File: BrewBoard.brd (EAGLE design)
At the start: 69.2 x 20.3 mm, 23 parts, among them J1 BATT, J2 AUX, J3 SPK, J5 PIXEL, J6 STAR, J7 MAIN, J8 String, Q1 2n7002k, Q2 2n7002k, Q3 2n7002k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

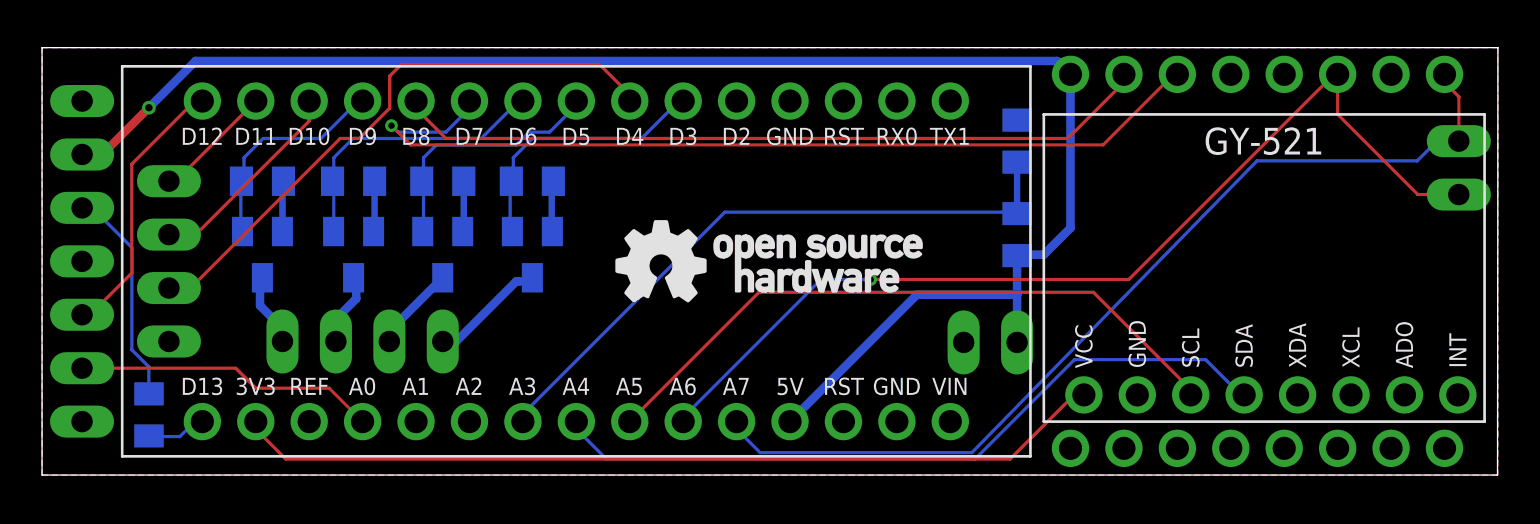
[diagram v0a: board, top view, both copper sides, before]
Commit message: Brewboard V3 Update
Adding New Version 3 Update of Brewboard
Feature/Change List;
- Interrupt mode is now available for clashes.
- All extra Pins have pads (for folks that want to experiment and add features).
- LED Power Traces are now able to handle a total of 7.8A so Pixel Blades can be safely hooked up to MOSFETs (less drain in deepsleep).
- Power Traces for Pixels removed! Pixel Blade can be wired directly from the battery Positive, and to two or three of the RGB MOSFET pads as mentioned above.
- 4th MOSFET removed to reduce part count.
- Pixel Data Line resistor removed, as it really should be on the blade side (also reduces part count).
- All Pins are now Labelled and should now be large enough to be readable.
- Added a few Vias for better overall grounds.
- Spiffy new logo!
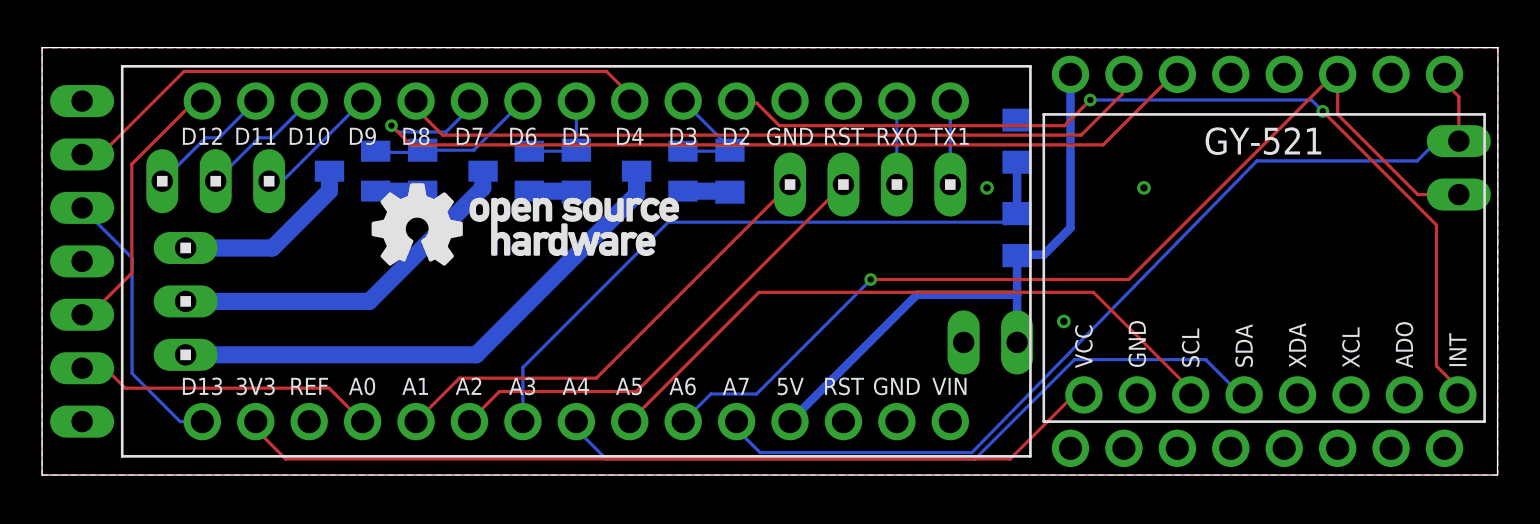
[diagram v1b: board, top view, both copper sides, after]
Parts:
- removed J2: AUX, BrewBoard:10X02MTA
- removed Q4: 2n7002k, BrewBoard:SOT23
- removed R4: 100k Ohms, BrewBoard:R0805
- removed R5: 220 Ohm, BrewBoard:R0805
- added J4: STAR, BrewBoard:10X03MTA
- added J9: COM, BrewBoard:10X02MTA
- J5: value PIXEL -> AUX
- J6: value STAR -> ANO; device BrewBoard:10X04MTA -> BrewBoard:10X02MTA
- J8: value String -> DIGI; device BrewBoard:10X02MTA -> BrewBoard:10X03MTA
- Q1, Q2, Q3: value 2n7002k -> si2302cds-t1-e3
- R6: value 100 kOhm -> 100k Ohms
- R7: value 470 kOhm -> 470k Ohms
- U$2: device BrewBoard:BREWBOARD-LOGO_VERYSMALL -> SaberRepublicLogos:BREWBOARD_GOLDSTAR_SM
- moved J6 22.8 mm to (36.8, 13.8), flipped to the top
- moved U$2 16.2 mm to (11.3, 4.45)
- moved U$3 11.7 mm to (15.7, 10.0)
- moved R1 9.40 mm to (32.7, 14.4), turned to 270 degrees
- moved Q3 7.24 mm to (29.4, 14.4), turned to 270 degrees
- moved R2 6.37 mm to (25.4, 14.4), turned to 270 degrees
- moved Q2 4.98 mm to (22.1, 14.4), turned to 270 degrees
- moved Q1 3.97 mm to (14.8, 14.4), turned to 270 degrees
- moved R3 3.32 mm to (18.1, 14.4), turned to 270 degrees
- moved J8 2.56 mm to (8.26, 14.0), flipped to the top, turned to 180 degrees
- renumbered U$1 to U3
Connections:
- net N$16 renamed D11
- net N$7 renamed D10
- removed net N$23: J6.2, Q1.3
- removed net N$24: J6.3, Q2.3
- removed net N$25: J6.4, Q3.3
- removed net N$28: J6.1, Q4.3
- removed net N$9: J5.3, R5.1
- new net A1: J6.2, U1.20
- new net A2: J6.1, U1.21
- new net D2: U1.5, U2.INT
- new net LS1: J4.3, Q3.3
- new net LS2: J4.2, Q2.3
- new net LS3: J4.1, Q1.3
- new net N$1: J9.2, U1.2
- new net N$2: J9.1, U1.1
- net +5V: no longer J5.2
- net 0: no longer J2.1, Q4.2, R4.2
- net D13: now also J5.3; no longer R5.2
- net D4: now also J5.2; no longer J2.2
- net D9: now also J8.3; no longer Q4.1, R4.1
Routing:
- net +5V: track 76.9 -> 27.8 mm, vias 1 -> 0
- net D2: track 0.00 -> 45.3 mm, vias 0 -> 2
- net LS1: track 0.00 -> 25.7 mm
- net A2: track 0.00 -> 22.4 mm
- net A1: track 0.00 -> 22.4 mm
- net LS2: track 0.00 -> 17.2 mm
- net N$9: track 10.6 -> 0.00 mm
- net D13: track 2.84 -> 13.1 mm
- net LS3: track 0.00 -> 8.90 mm
- net D3: track 12.9 -> 5.51 mm
- net D5: track 12.1 -> 5.25 mm
- net D6: track 13.7 -> 8.02 mm
- net N$25: track 5.50 -> 0.00 mm
- net D9: track 10.4 -> 6.02 mm
- net N$24: track 4.16 -> 0.00 mm
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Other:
- board text added: "A1"
- board text added: "A2"
- board text added: "BLU"
- board text added: "DAT"
- board text added: "GRN"
- board text added: "LS4"
- board text added: "RED"
- board text added: "RX"
- board text added: "TX"
- board text added: "V3.0.1-C1"
- board text removed: "B/LS3"
- board text removed: "DATA"
- board text removed: "G/LS2"
- board text removed: "R/LS1"
- board text removed: "V2.0.1-C1"
- board text removed: "VCC"
- board text removed: "W/LS4"

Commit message: Updated to V4
Updated source files to V4 and deleted PDF version of Schematic
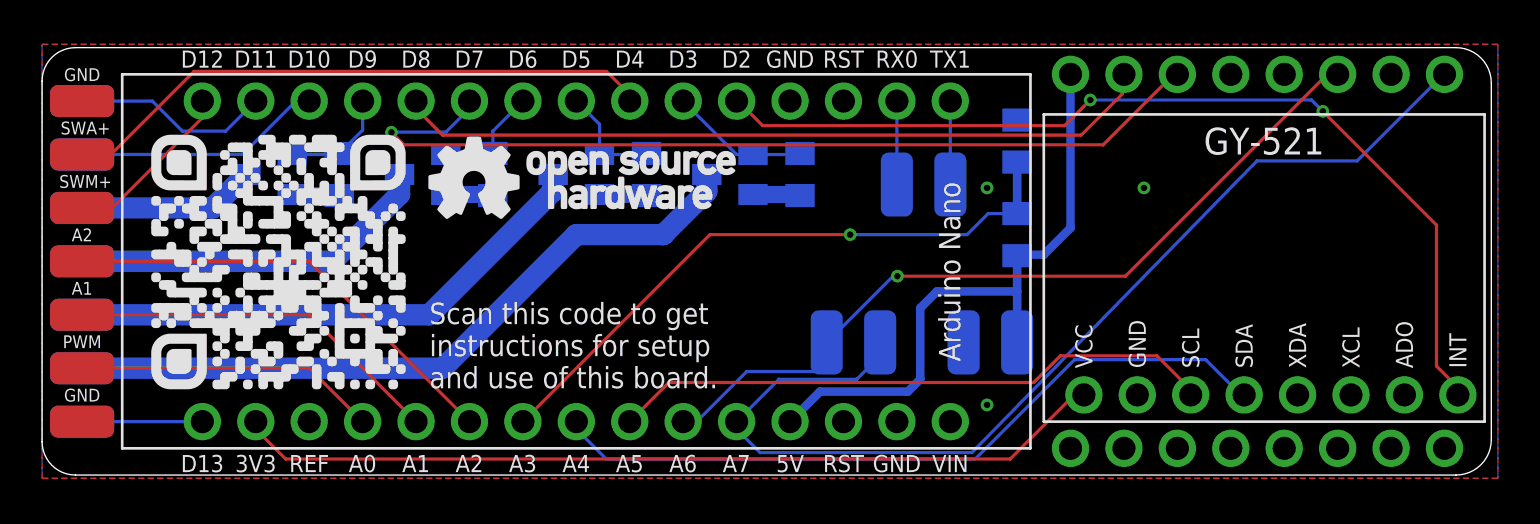
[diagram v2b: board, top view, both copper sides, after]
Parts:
- removed J1: BATT, BrewBoard:10X02MTA
- removed J3: SPK, BrewBoard:10X02MTA
- removed J4: STAR, BrewBoard:10X03MTA
- removed J5: AUX, BrewBoard:10X03MTA
- removed J6: ANO, BrewBoard:10X02MTA
- removed J7: MAIN, BrewBoard:10X04MTA
- removed J8: DIGI, BrewBoard:10X03MTA
- removed J9: COM, BrewBoard:10X02MTA
- added LS1, SPK+, U$1, U$11, U$12, U$13, U$15, U$16, U$17, U$18, U$19, U$22, U$27, U$28, U$4, U$5, U$6, U$7, U$8, U$9: SINGLE_ONE_SIDE_PAD, BrewboardV4:SOS_PAD
- added Q4: si2302cds-t1-e3, BrewBoard:SOT23
- added R4: 100k Ohms, BrewBoard:R0805
- added U$31: (no value), SaberRepublicLogos:BREWBOARD_QR_CODE
- U1: device BrewBoard:ARDUINO_NANO -> BrewBoard:ARDUINO_NANO_OUT
- moved Q1 17.9 mm to (32.7, 14.3)
- moved Q3 11.3 mm to (18.1, 14.3)
- moved U$3 3.50 mm to (18.4, 12.2)
- moved R1 3.34 mm to (36.0, 14.3)
- moved R2 3.34 mm to (28.7, 14.3)
- moved Q2 3.34 mm to (25.4, 14.3)
- moved R3 3.34 mm to (21.4, 14.3)
- moved U$2 0.32 mm to (11.0, 4.45)
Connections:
- net N$14 renamed A3
- removed net N$1: J9.2, U1.2
- removed net N$2: J9.1, U1.1
- new net D0: U$5.P$1, U1.2
- new net D1: U$6.P$1, U1.1
- new net LS4: Q4.3, U$7.P$1
- net +5V: now also U$12.P$1; no longer J1.2
- net 0: now also Q4.2, R4.2, U$13.P$1, U$17.P$1, U$27.P$1; no longer J1.1, J5.1, J7.1, J7.4
- net A0: now also U$18.P$1; no longer J7.3
- net A1: now also U$1.P$1; no longer J6.2
- net A2: now also U$4.P$1; no longer J6.1
- net A6: now also U$11.P$1; no longer J3.1
- net A7: now also SPK+.P$1; no longer J3.2
- net D10: now also U$8.P$1; no longer J8.2
- net D11: now also U$9.P$1; no longer J8.1
- net D12: now also U$19.P$1; no longer J7.2
- net D13: now also U$28.P$1; no longer J5.3
- net D3: now also Q1.1; no longer Q3.1
- net D4: now also U$22.P$1; no longer J5.2
- net D6: now also Q3.1; no longer Q1.1
- net D9: now also Q4.1, R4.1; no longer J8.3
- net LS1: now also LS1.P$1, Q1.3; no longer J4.3, Q3.3
- net LS2: now also U$15.P$1; no longer J4.2
- net LS3: now also Q3.3, U$16.P$1; no longer J4.1, Q1.3
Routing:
- net LS3: track 8.90 -> 17.4 mm
- net LS2: track 17.2 -> 25.7 mm
- net LS4: track 0.00 -> 8.45 mm
- net A6: track 47.2 -> 38.8 mm
- net LS1: track 25.7 -> 34.0 mm
- net D13: track 13.1 -> 5.71 mm
- net A7: track 44.9 -> 51.2 mm
- net D10: track 6.02 -> 11.8 mm
- net D12: track 13.0 -> 8.28 mm
- net A1: track 22.4 -> 18.3 mm
- net N$2: track 3.97 -> 0.00 mm
- net N$1: track 3.97 -> 0.00 mm
- net D1: track 0.00 -> 3.97 mm
- net D0: track 0.00 -> 3.97 mm
- net D11: track 6.02 -> 9.44 mm
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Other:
- board size 69.2 x 20.3 mm -> 68.9 x 20.3 mm
- board text added: "Arduino Nano"
- board text added: "PWR"
- board text added: "SPK"
- board text added: "SWA+"
- board text added: "SWM+"
- board text added: "Scan this code to get instructions for setup and use of this board."
- board text added: "V4.0.1-B3"
- board text removed: "SW+"
- board text removed: "V3.0.1-C1"
